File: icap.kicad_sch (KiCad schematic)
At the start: 7 parts

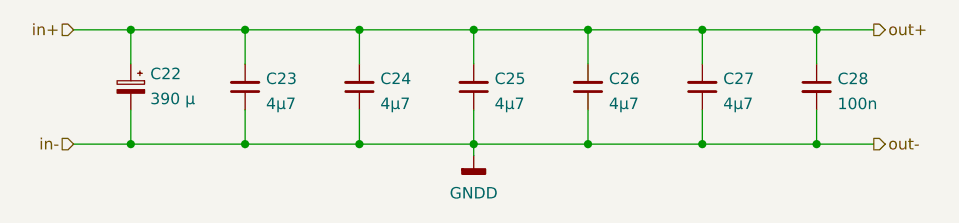
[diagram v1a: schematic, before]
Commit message: Clean up schematic
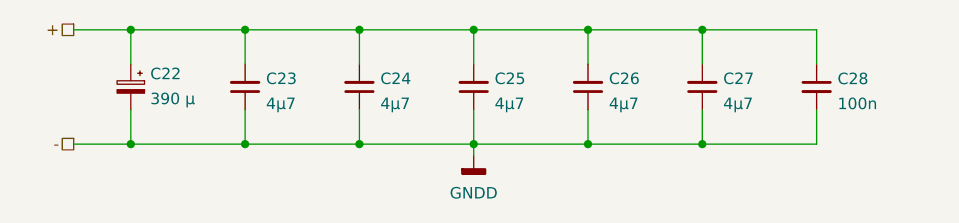
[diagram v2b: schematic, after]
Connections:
- net in+ renamed +
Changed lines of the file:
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@@
 (kicad_sch (version 20211123) (generator eeschema)
   (paper "A4")
-  (junction (at 114.3 114.3) (diameter 0) (color 0 0 0 0)
+  (junction (at 114.3 101.6) (diameter 0) (color 0 0 0 0)
   )
   (junction (at 177.8 101.6) (diameter 0) (color 0 0 0 0)
-  )
-  (junction (at 190.5 101.6) (diameter 0) (color 0 0 0 0)
   )
   (junction (at 127 101.6) (diameter 0) (color 0 0 0 0)
@@
   (junction (at 139.7 114.3) (diameter 0) (color 0 0 0 0)
   )
-  (junction (at 190.5 114.3) (diameter 0) (color 0 0 0 0)
-  )
   (junction (at 152.4 101.6) (diameter 0) (color 0 0 0 0)
   )
   (junction (at 165.1 114.3) (diameter 0) (color 0 0 0 0)
+  )
+  (junction (at 114.3 114.3) (diameter 0) (color 0 0 0 0)
   )
   (junction (at 139.7 101.6) (diameter 0) (color 0 0 0 0)
@@
   )
   (junction (at 152.4 114.3) (diameter 0) (color 0 0 0 0)
-  )
-  (junction (at 114.3 101.6) (diameter 0) (color 0 0 0 0)
-  )
-  (wire (pts (xy 152.4 115.57) (xy 152.4 114.3))
-    (stroke (width 0) (type default) (color 0 0 0 0))
   )
   (wire (pts (xy 139.7 114.3) (xy 139.7 110.49))
@@
     (stroke (width 0) (type default) (color 0 0 0 0))
   )
-  (wire (pts (xy 190.5 101.6) (xy 196.85 101.6))
+  (wire (pts (xy 107.95 101.6) (xy 114.3 101.6))
     (stroke (width 0) (type default) (color 0 0 0 0))
   )
@@
     (stroke (width 0) (type default) (color 0 0 0 0))
   )
-  (wire (pts (xy 190.5 114.3) (xy 196.85 114.3))
-    (stroke (width 0) (type default) (color 0 0 0 0))
-  )
   (wire (pts (xy 127 110.49) (xy 127 114.3))
     (stroke (width 0) (type default) (color 0 0 0 0))
@@
   )
   (wire (pts (xy 139.7 105.41) (xy 139.7 101.6))
+    (stroke (width 0) (type default) (color 0 0 0 0))
+  )
+  (wire (pts (xy 107.95 114.3) (xy 114.3 114.3))
     (stroke (width 0) (type default) (color 0 0 0 0))
   )
@@
     (stroke (width 0) (type default) (color 0 0 0 0))
   )
-  (wire (pts (xy 107.95 114.3) (xy 114.3 114.3))
-    (stroke (width 0) (type default) (color 0 0 0 0))
-  )
   (wire (pts (xy 165.1 101.6) (xy 177.8 101.6))
     (stroke (width 0) (type default) (color 0 0 0 0))
@@
     (stroke (width 0) (type default) (color 0 0 0 0))
   )
-  (wire (pts (xy 107.95 101.6) (xy 114.3 101.6))
-    (stroke (width 0) (type default) (color 0 0 0 0))
-  )
   (wire (pts (xy 177.8 101.6) (xy 177.8 105.41))
     (stroke (width 0) (type default) (color 0 0 0 0))
   )
   (wire (pts (xy 190.5 114.3) (xy 177.8 114.3))
+    (stroke (width 0) (type default) (color 0 0 0 0))
+  )
+  (wire (pts (xy 152.4 114.3) (xy 152.4 115.57))
     (stroke (width 0) (type default) (color 0 0 0 0))
   )
@@
     (stroke (width 0) (type default) (color 0 0 0 0))
   )
-  (hierarchical_label "in-" (shape input) (at 107.95 114.3 180)
+  (hierarchical_label "-" (shape passive) (at 107.95 114.3 180)
     (effects (font (size 1.27 1.27)) (justify right))
   )
-  (hierarchical_label "out+" (shape output) (at 196.85 101.6 0)
-    (effects (font (size 1.27 1.27)) (justify left))
-  )
-  (hierarchical_label "in+" (shape input) (at 107.95 101.6 180)
+  (hierarchical_label "+" (shape passive) (at 107.95 101.6 180)
     (effects (font (size 1.27 1.27)) (justify right))
-  )
-  (hierarchical_label "out-" (shape output) (at 196.85 114.3 0)
-    (effects (font (size 1.27 1.27)) (justify left))
   )
   (symbol (lib_id "Device:C_Small") (at 127 107.95 180) (unit 1)
@@
   (symbol (lib_id "power:GNDD") (at 152.4 115.57 0) (unit 1)
     (in_bom yes) (on_board yes) (fields_autoplaced)
-    (property "Reference" "#PWR066" (id 0) (at 152.4 121.92 0)
+    (property "Reference" "#PWR0101" (id 0) (at 152.4 121.92 0)
       (effects (font (size 1.27 1.27)) hide)
     )

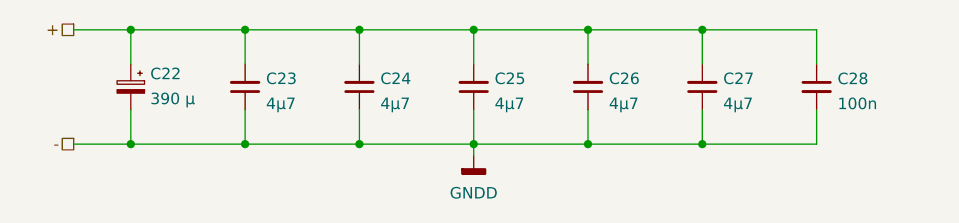
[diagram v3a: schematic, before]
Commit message: Add separate ADCs for remote measurements
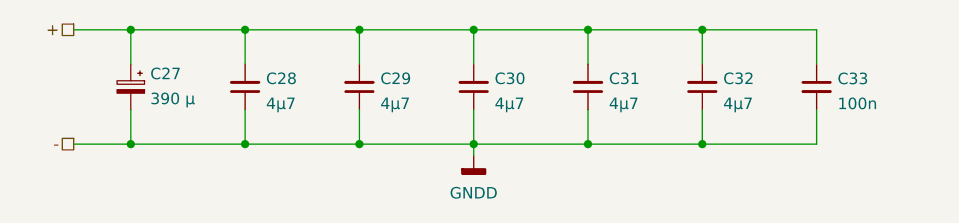
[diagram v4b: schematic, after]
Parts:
- C33: renamed from C28; footprint Capacitor_SMD:C_0402_1005Metric -> Capacitor_SMD:C_0603_1608Metric; Manufacturer Murata -> Taiyo Yuden; Part Number GRM155R72A102KA01J -> HMK107B7104KA
- renumbered C22 to C27, C23 to C28, C24 to C29, C25 to C30, C26 to C31, C27 to C32
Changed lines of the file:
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@@
   (symbol (lib_id "Device:C_Small") (at 127 107.95 180) (unit 1)
     (in_bom yes) (on_board yes) (fields_autoplaced)
-    (property "Reference" "C23" (id 0) (at 129.3241 107.0351 0)
+    (property "Reference" "C28" (id 0) (at 129.3241 107.0351 0)
       (effects (font (size 1.27 1.27)) (justify right))
     )
@@
   (symbol (lib_id "Device:C_Small") (at 177.8 107.95 180) (unit 1)
     (in_bom yes) (on_board yes) (fields_autoplaced)
-    (property "Reference" "C27" (id 0) (at 180.1241 107.0351 0)
+    (property "Reference" "C32" (id 0) (at 180.1241 107.0351 0)
       (effects (font (size 1.27 1.27)) (justify right))
     )
@@
   (symbol (lib_id "power:GNDD") (at 152.4 115.57 0) (unit 1)
     (in_bom yes) (on_board yes) (fields_autoplaced)
-    (property "Reference" "#PWR066" (id 0) (at 152.4 121.92 0)
+    (property "Reference" "#PWR090" (id 0) (at 152.4 121.92 0)
       (effects (font (size 1.27 1.27)) hide)
     )
@@
   (symbol (lib_id "Device:C_Polarized_Small") (at 114.3 107.95 0) (mirror y) (unit 1)
     (in_bom yes) (on_board yes) (fields_autoplaced)
-    (property "Reference" "C22" (id 0) (at 116.459 106.4954 0)
+    (property "Reference" "C27" (id 0) (at 116.459 106.4954 0)
       (effects (font (size 1.27 1.27)) (justify right))
     )
@@
   (symbol (lib_id "Device:C_Small") (at 165.1 107.95 180) (unit 1)
     (in_bom yes) (on_board yes) (fields_autoplaced)
-    (property "Reference" "C26" (id 0) (at 167.4241 107.0351 0)
+    (property "Reference" "C31" (id 0) (at 167.4241 107.0351 0)
       (effects (font (size 1.27 1.27)) (justify right))
     )
@@
   (symbol (lib_id "Device:C_Small") (at 152.4 107.95 180) (unit 1)
     (in_bom yes) (on_board yes) (fields_autoplaced)
-    (property "Reference" "C25" (id 0) (at 154.7241 107.0351 0)
+    (property "Reference" "C30" (id 0) (at 154.7241 107.0351 0)
       (effects (font (size 1.27 1.27)) (justify right))
     )
@@
   (symbol (lib_id "Device:C_Small") (at 190.5 107.95 0) (unit 1)
     (in_bom yes) (on_board yes) (fields_autoplaced)
-    (property "Reference" "C28" (id 0) (at 192.8241 107.0478 0)
+    (property "Reference" "C33" (id 0) (at 192.8241 107.0478 0)
       (effects (font (size 1.27 1.27)) (justify left))
     )
@@
       (effects (font (size 1.27 1.27)) (justify left))
     )
-    (property "Footprint" "Capacitor_SMD:C_0402_1005Metric" (id 2) (at 190.5 107.95 0)
+    (property "Footprint" "Capacitor_SMD:C_0603_1608Metric" (id 2) (at 190.5 107.95 0)
       (effects (font (size 1.27 1.27)) hide)
     )
@@
       (effects (font (size 1.27 1.27)) hide)
     )
-    (property "Manufacturer" "Murata" (id 4) (at 190.5 107.95 0)
+    (property "Manufacturer" "Taiyo Yuden" (id 4) (at 190.5 107.95 0)
       (effects (font (size 1.27 1.27)) hide)
     )
-    (property "Part Number" "GRM155R72A102KA01J" (id 5) (at 190.5 107.95 0)
+    (property "Part Number" " HMK107B7104KA" (id 5) (at 190.5 107.95 0)
       (effects (font (size 1.27 1.27)) hide)
     )
@@
   (symbol (lib_id "Device:C_Small") (at 139.7 107.95 180) (unit 1)
     (in_bom yes) (on_board yes) (fields_autoplaced)
-    (property "Reference" "C24" (id 0) (at 142.0241 107.0351 0)
+    (property "Reference" "C29" (id 0) (at 142.0241 107.0351 0)
       (effects (font (size 1.27 1.27)) (justify right))
     )

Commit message: Add 100 nF bypass capacitor to ESP32 power input
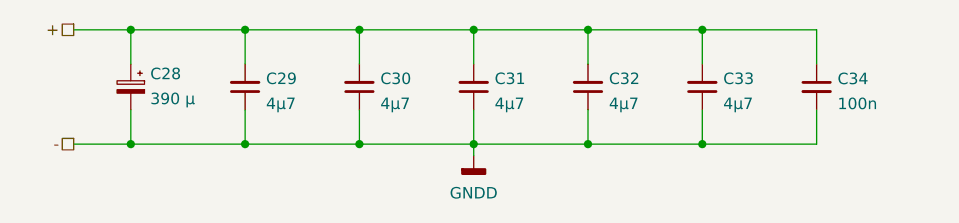
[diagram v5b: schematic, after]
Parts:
- renumbered C27 to C28, C28 to C29, C29 to C30, C30 to C31, C31 to C32, C32 to C33, C33 to C34
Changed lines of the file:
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@@
   (symbol (lib_id "Device:C_Small") (at 127 107.95 180) (unit 1)
     (in_bom yes) (on_board yes) (fields_autoplaced)
-    (property "Reference" "C28" (id 0) (at 129.3241 107.0351 0)
+    (property "Reference" "C29" (id 0) (at 129.3241 107.0351 0)
       (effects (font (size 1.27 1.27)) (justify right))
     )
@@
   (symbol (lib_id "Device:C_Small") (at 177.8 107.95 180) (unit 1)
     (in_bom yes) (on_board yes) (fields_autoplaced)
-    (property "Reference" "C32" (id 0) (at 180.1241 107.0351 0)
+    (property "Reference" "C33" (id 0) (at 180.1241 107.0351 0)
       (effects (font (size 1.27 1.27)) (justify right))
     )
@@
   (symbol (lib_id "power:GNDD") (at 152.4 115.57 0) (unit 1)
     (in_bom yes) (on_board yes) (fields_autoplaced)
-    (property "Reference" "#PWR090" (id 0) (at 152.4 121.92 0)
+    (property "Reference" "#PWR091" (id 0) (at 152.4 121.92 0)
       (effects (font (size 1.27 1.27)) hide)
     )
@@
   (symbol (lib_id "Device:C_Polarized_Small") (at 114.3 107.95 0) (mirror y) (unit 1)
     (in_bom yes) (on_board yes) (fields_autoplaced)
-    (property "Reference" "C27" (id 0) (at 116.459 106.4954 0)
+    (property "Reference" "C28" (id 0) (at 116.459 106.4954 0)
       (effects (font (size 1.27 1.27)) (justify right))
     )
@@
   (symbol (lib_id "Device:C_Small") (at 165.1 107.95 180) (unit 1)
     (in_bom yes) (on_board yes) (fields_autoplaced)
-    (property "Reference" "C31" (id 0) (at 167.4241 107.0351 0)
+    (property "Reference" "C32" (id 0) (at 167.4241 107.0351 0)
       (effects (font (size 1.27 1.27)) (justify right))
     )
@@
   (symbol (lib_id "Device:C_Small") (at 152.4 107.95 180) (unit 1)
     (in_bom yes) (on_board yes) (fields_autoplaced)
-    (property "Reference" "C30" (id 0) (at 154.7241 107.0351 0)
+    (property "Reference" "C31" (id 0) (at 154.7241 107.0351 0)
       (effects (font (size 1.27 1.27)) (justify right))
     )
@@
   (symbol (lib_id "Device:C_Small") (at 190.5 107.95 0) (unit 1)
     (in_bom yes) (on_board yes) (fields_autoplaced)
-    (property "Reference" "C33" (id 0) (at 192.8241 107.0478 0)
+    (property "Reference" "C34" (id 0) (at 192.8241 107.0478 0)
       (effects (font (size 1.27 1.27)) (justify left))
     )
@@
   (symbol (lib_id "Device:C_Small") (at 139.7 107.95 180) (unit 1)
     (in_bom yes) (on_board yes) (fields_autoplaced)
-    (property "Reference" "C29" (id 0) (at 142.0241 107.0351 0)
+    (property "Reference" "C30" (id 0) (at 142.0241 107.0351 0)
       (effects (font (size 1.27 1.27)) (justify right))
     )
